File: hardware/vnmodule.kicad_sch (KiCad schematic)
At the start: 4 parts

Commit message: Fixes after review
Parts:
- R7: value 1k -> 33R
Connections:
- net GNSS_SYNC: now reaches U1.29 (GNSS_SYNC)
- net SNC_IN: no longer names the net of U1.22 (SYNC_IN)
- net SNC_OUT: no longer names the net of U1.9 (SYNC_OUT)
- no-connect marks 3 -> 4
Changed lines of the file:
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@@
+	)
+	(no_connect
+		(at 151.13 90.17)
+	)
+	(no_connect
+		(at 151.13 87.63)
 	)
 	(no_connect
@@
 		(at 151.13 78.74)
 	)
-	(no_connect
-		(at 100.33 93.98)
-	)
 	(wire
 		(pts
@@
 	(wire
 		(pts
-			(xy 157.48 90.17) (xy 151.13 90.17)
-		)
-		(stroke
-			(width 0)
-			(type default)
-		)
-	)
-	(wire
-		(pts
 			(xy 128.27 123.19) (xy 128.27 125.73)
 		)
@@
 	(wire
 		(pts
+			(xy 93.98 93.98) (xy 100.33 93.98)
+		)
+		(stroke
+			(width 0)
+			(type default)
+		)
+	)
+	(wire
+		(pts
 			(xy 64.77 91.44) (xy 64.77 95.25)
 		)
@@
 		(pts
 			(xy 125.73 123.19) (xy 125.73 125.73)
-		)
-		(stroke
-			(width 0)
-			(type default)
-		)
-	)
-	(wire
-		(pts
-			(xy 157.48 87.63) (xy 151.13 87.63)
 		)
 		(stroke
@@
 		)
 	)
-	(hierarchical_label "SNC_IN"
+	(hierarchical_label "GNSS_SYNC"
 		(shape input)
-		(at 157.48 90.17 0)
-		(effects
-			(font
-				(size 1.27 1.27)
-			)
-			(justify left)
+		(at 93.98 93.98 180)
+		(effects
+			(font
+				(size 1.27 1.27)
+			)
+			(justify right)
 		)
 	)
@@
 			)
 			(justify right)
-		)
-	)
-	(hierarchical_label "SNC_OUT"
-		(shape output)
-		(at 157.48 87.63 0)
-		(effects
-			(font
-				(size 1.27 1.27)
-			)
-			(justify left)
 		)
 	)
@@
 			)
 		)
-		(property "Value" "1k"
-			(at 162.814 101.6 90)
-			(effects
-				(font
+		(property "Value" "33R"
+			(at 163.322 101.6 90)
+			(effects
+				(font

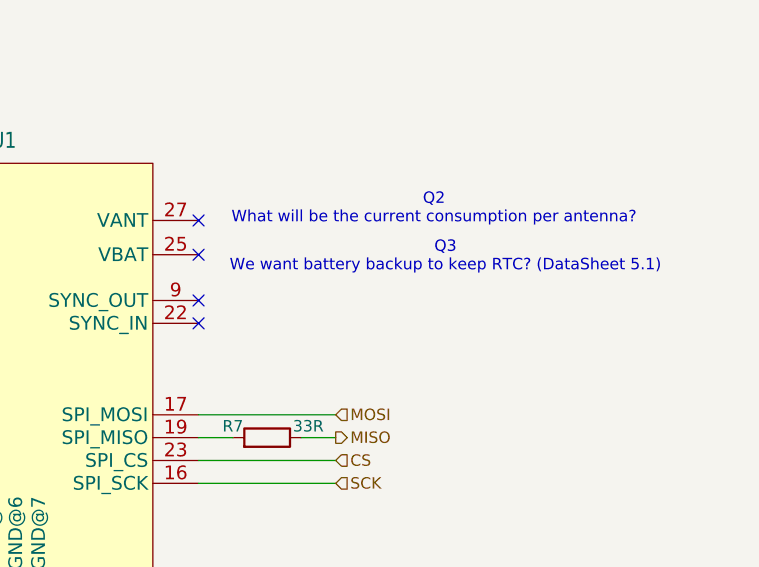
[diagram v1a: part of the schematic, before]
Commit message: Added pi-filter to VANT and added socket for battery
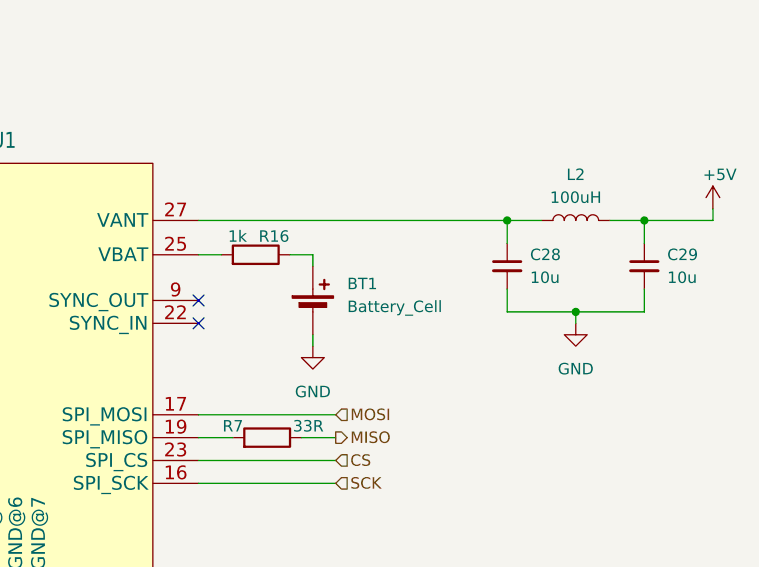
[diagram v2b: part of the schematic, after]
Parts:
- added BT1: Battery_Cell, Battery:BatteryHolder_Keystone_2998_1x6.8mm, symbol Device:Battery_Cell
- added C28, C29: 10u, 10uCap:CAPC3225X280N, symbol Device:C_Small
- added L2: 100uH, symbol Device:L
- added R16: 1k, symbol Device:R
- U1: value ~ -> (none)
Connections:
- net GND: now also BT1.2 (-), C28.2, C29.2
- net at U1.25 (VBAT): now also R16.2
- net at U1.27 (VANT): now also C28.1, L2.1
- new net: BT1.1 (+), R16.1
- new net +5V: C29.1, L2.2
- no-connect marks 4 -> 2
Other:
- note removed: "Q2 What will be the current consumption per antenna?"
- note removed: "Q3 We want battery backup to keep RTC? (DataSheet 5.1)"

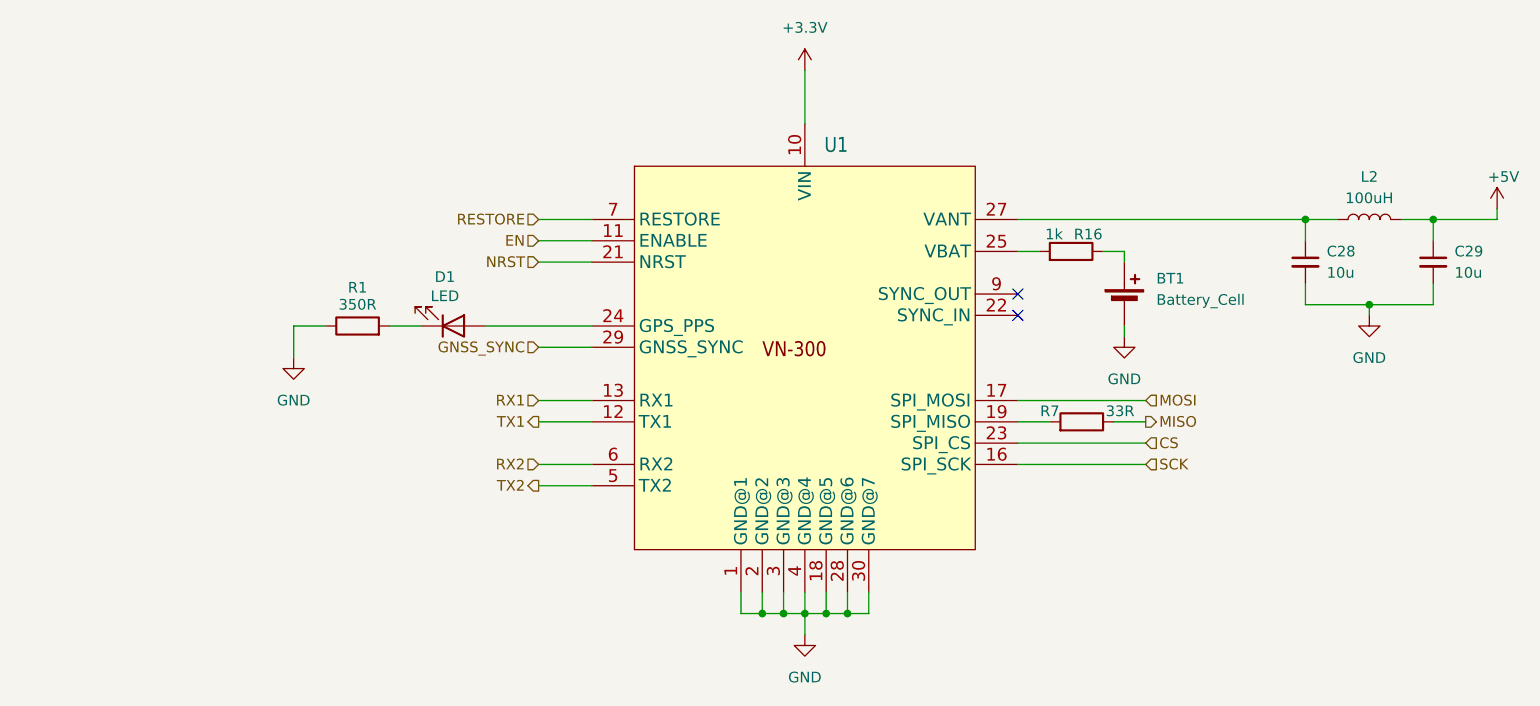
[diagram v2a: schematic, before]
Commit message: Fixes after review and mouser links for most components added
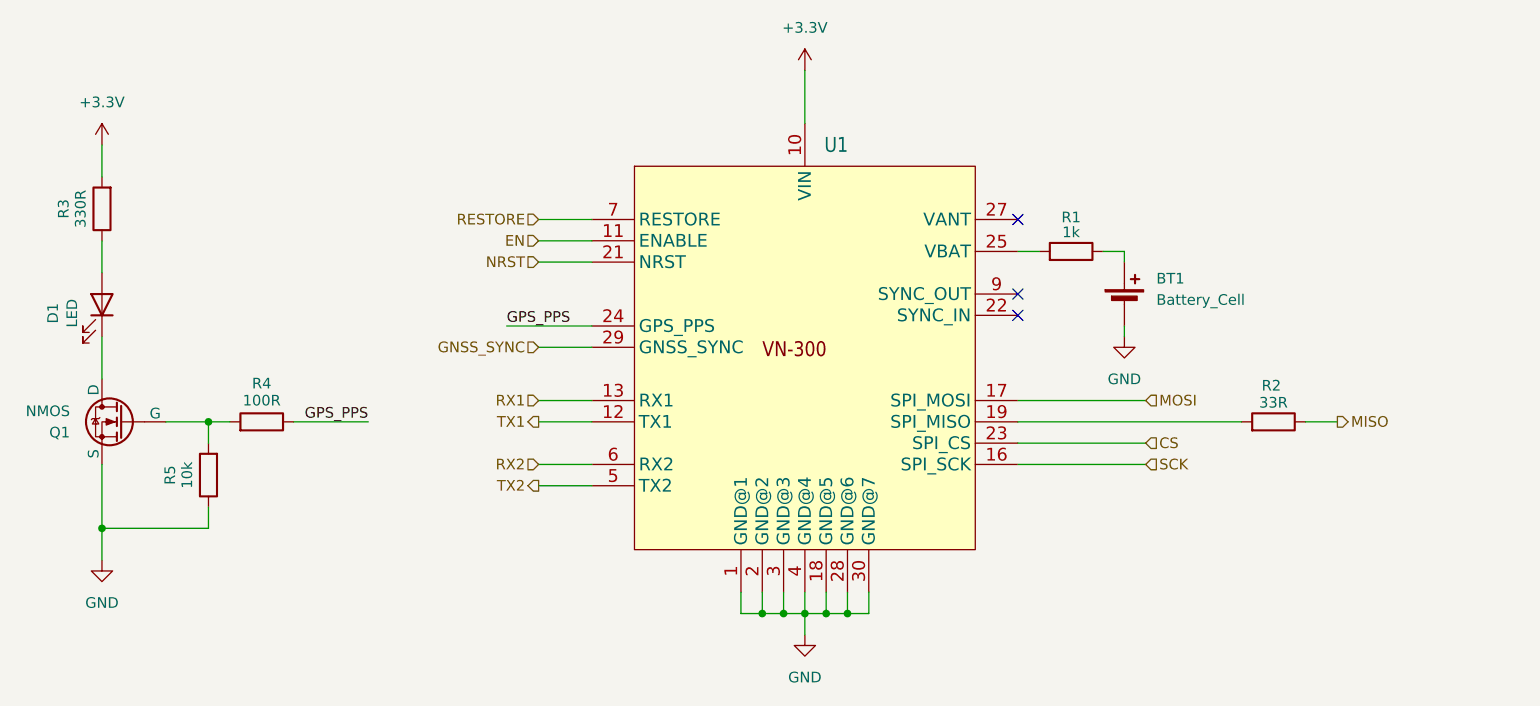
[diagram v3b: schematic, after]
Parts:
- removed C28, C29: 10u, 10uCap:CAPC3225X280N, symbol Device:C_Small
- removed L2: 100uH, symbol Device:L
- removed R1: 350R, symbol Device:R
- added Q1: NMOS, VNlednmos:DMN63D8L13, symbol Simulation_SPICE:NMOS
- added R3: 330R, Resistor_SMD:R_0603_1608Metric_Pad0.98x0.95mm_HandSolder, symbol Device:R
- added R4: 100R, Resistor_SMD:R_0603_1608Metric_Pad0.98x0.95mm_HandSolder, symbol Device:R
- added R5: 10k, Resistor_SMD:R_0603_1608Metric_Pad0.98x0.95mm_HandSolder, symbol Device:R
- R1: renamed from R16; footprint (none) -> Resistor_SMD:R_0603_1608Metric_Pad0.98x0.95mm_HandSolder; Mouser (none) -> https://www.mouser.pl/ProductDetail/Vishay/CRCW06031K00FKEE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
- R2: renamed from R7; footprint (none) -> Resistor_SMD:R_0603_1608Metric_Pad0.98x0.95mm_HandSolder; Mouser (none) -> https://www.mouser.pl/ProductDetail/YAGEO/RC0603FR-7W33RL?q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
- U1: value (none) -> VN-300; Mouser (none) -> ---
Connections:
- net +3.3V: now also R3.2
- net GND: now also Q1.3 (S), R5.1
- net at D1.1 (K): now also Q1.1 (D)
- net at D1.2 (A): now also R3.1; no longer U1.24 (GPS_PPS)
- new net: Q1.2 (G), R4.2, R5.2
- new net GPS_PPS: R4.1, U1.24 (GPS_PPS)
- no-connect marks 2 -> 3
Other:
- moved on the sheet: D1, R2

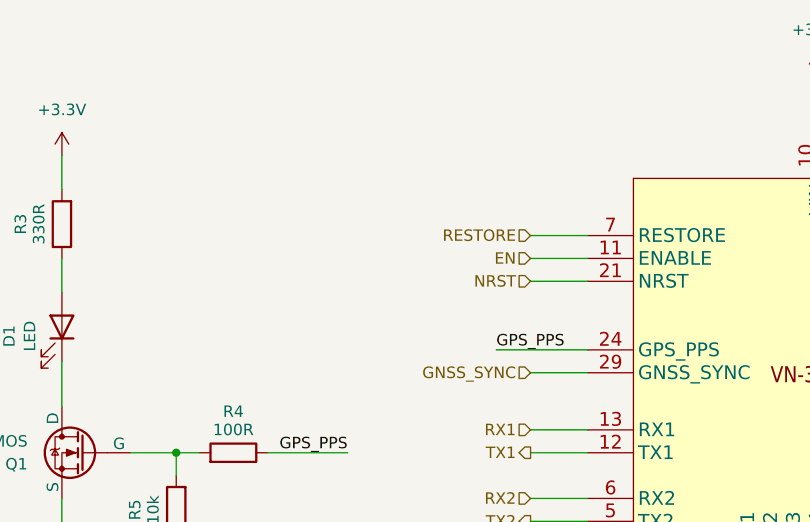
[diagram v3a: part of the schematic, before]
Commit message: changed some elements on shematic
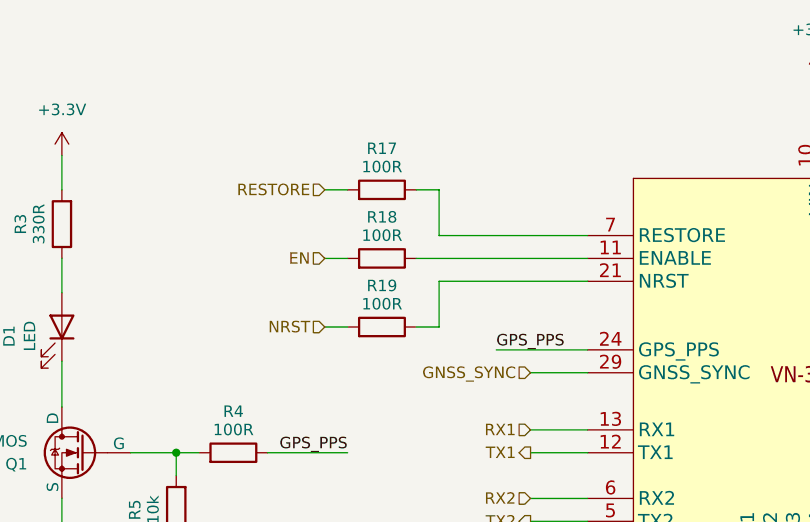
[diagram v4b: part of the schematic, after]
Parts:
- added R17, R18, R19: 100R, Resistor_SMD:R_0603_1608Metric_Pad0.98x0.95mm_HandSolder, symbol Device:R
- D1: footprint (none) -> Diode_SMD:D_0603_1608Metric_Pad1.05x0.95mm_HandSolder; Mouser (none) -> https://www.mouser.pl/ProductDetail/Wurth-Elektronik/150060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
- U1: footprint (none) -> vectornav:7X8CASTLE
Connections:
- net EN: now also R18.2; no longer U1.11 (ENABLE)
- net NRST: now also R19.2; no longer U1.21 (NRST)
- net RESTORE: now also R17.2; no longer U1.7 (RESTORE)
- new net: R18.1, U1.11 (ENABLE)
- new net: R19.1, U1.21 (NRST)
- new net: R17.1, U1.7 (RESTORE)

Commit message: 3D models, optocoupler added, pcb settings and components placing
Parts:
- BT1: footprint Battery:BatteryHolder_Keystone_2998_1x6.8mm -> BatteryHolder:2998TR; Mouser (none) -> https://www.mouser.pl/ProductDetail/Keystone-Electronics/29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
- U1: footprint vectornav:7X8CASTLE -> VN300:7X8CASTLE
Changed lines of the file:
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@@
+	)
+	(junction
+		(at 130.81 125.73)
+		(diameter 0)
+		(color 0 0 0 0)
+	)
+	(junction
+		(at 125.73 125.73)
+		(diameter 0)
+		(color 0 0 0 0)
 	)
 	(junction
@@
 	)
 	(junction
-		(at 125.73 125.73)
-		(diameter 0)
-		(color 0 0 0 0)
-	)
-	(junction
 		(at 123.19 125.73)
 		(diameter 0)
@@
 	(junction
 		(at 41.91 115.57)
-		(diameter 0)
-		(color 0 0 0 0)
-	)
-	(junction
-		(at 130.81 125.73)
 		(diameter 0)
 		(color 0 0 0 0)
@@
 			)
 		)
+		(property "Sim.Device" ""
+			(at 41.91 88.9 0)
+			(hide yes)
+			(show_name no)
+			(do_not_autoplace no)
+			(effects
+				(font
+					(size 1.27 1.27)
+				)
+			)
+		)
+		(property "Sim.Type" ""
+			(at 41.91 88.9 0)
+			(hide yes)
+			(show_name no)
+			(do_not_autoplace no)
+			(effects
+				(font
+					(size 1.27 1.27)
+				)
+			)
+		)
 		(pin "2"
 		)
@@
 			)
 		)
+		(property "Sim.Device" ""
+			(at 44.45 102.87 0)
+			(hide yes)
+			(show_name no)
+			(do_not_autoplace no)
+			(effects
+				(font
+					(size 1.27 1.27)
+				)
+			)
+		)
+		(property "Sim.Type" ""
+			(at 44.45 102.87 0)
+			(hide yes)
+			(show_name no)
+			(do_not_autoplace no)
+			(effects
+				(font
+					(size 1.27 1.27)
+				)
+			)
+		)
 		(pin "3"
 		)
@@
 		)
 		(property "Manufacturer" ""
+			(at 54.61 109.22 90)
+			(hide yes)
+			(show_name no)
+			(do_not_autoplace no)
+			(effects
+				(font
+					(size 1.27 1.27)
+				)
+			)
+		)
+		(property "Sim.Device" ""
+			(at 54.61 109.22 90)
+			(hide yes)
+			(show_name no)
+			(do_not_autoplace no)
+			(effects
+				(font
+					(size 1.27 1.27)
+				)
+			)
+		)
+		(property "Sim.Type" ""
 			(at 54.61 109.22 90)
 			(hide yes)
@@
 			)
 		)
+		(property "Sim.Device" ""
+			(at 157.48 82.55 90)
+			(hide yes)
+			(show_name no)
+			(do_not_autoplace no)
+			(effects
+				(font
+					(size 1.27 1.27)
+				)
+			)
+		)
+		(property "Sim.Type" ""
+			(at 157.48 82.55 90)
+			(hide yes)
+			(show_name no)
+			(do_not_autoplace no)
+			(effects
+				(font
+					(size 1.27 1.27)
+				)
+			)
+		)
 		(pin "2"
 		)
@@
 			)
 		)
-		(property "Footprint" "vectornav:7X8CASTLE"
+		(property "Footprint" "VN300:7X8CASTLE"
 			(at 123.952 99.314 0)
 			(hide yes)
@@
 		)
 		(property "Mouser" "---"
+			(at 125.73 95.25 0)
+			(hide yes)
+			(show_name no)
+			(do_not_autoplace no)
+			(effects
+				(font
+					(size 1.27 1.27)
+				)
+			)
+		)
+		(property "Sim.Device" ""
+			(at 125.73 95.25 0)
+			(hide yes)
+			(show_name no)
+			(do_not_autoplace no)
+			(effects
+				(font
+					(size 1.27 1.27)
+				)
+			)
+		)
+		(property "Sim.Type" ""
 			(at 125.73 95.25 0)
 			(hide yes)
@@
 			)
 		)
+		(property "Sim.Device" ""
+			(at 77.47 73.66 90)
+			(hide yes)
+			(show_name no)
+			(do_not_autoplace no)
+			(effects
+				(font
+					(size 1.27 1.27)
+				)
+			)
+		)
+		(property "Sim.Type" ""
+			(at 77.47 73.66 90)
+			(hide yes)
+			(show_name no)
+			(do_not_autoplace no)
+			(effects
+				(font
+					(size 1.27 1.27)
+				)
+			)
+		)
 		(pin "2"
 		)
@@
 			)
 		)
+		(property "Sim.Device" ""
+			(at 60.96 102.87 90)
+			(hide yes)
+			(show_name no)
+			(do_not_autoplace no)
+			(effects
+				(font
+					(size 1.27 1.27)
+				)
+			)
+		)
+		(property "Sim.Type" ""
+			(at 60.96 102.87 90)
+			(hide yes)
+			(show_name no)
+			(do_not_autoplace no)
+			(effects
+				(font
+					(size 1.27 1.27)
+				)
+			)
+		)
 		(pin "2"
 		)
@@
 			)
 		)
+		(property "Sim.Device" ""
+			(at 77.47 88.9 90)
+			(hide yes)
+			(show_name no)
+			(do_not_autoplace no)
+			(effects
+				(font
+					(size 1.27 1.27)
+				)
+			)
+		)
+		(property "Sim.Type" ""
+			(at 77.47 88.9 90)
+			(hide yes)
+			(show_name no)
+			(do_not_autoplace no)
+			(effects
+				(font
+					(size 1.27 1.27)
+				)
+			)
+		)
 		(pin "2"
 		)
@@
 		)
 		(property "Manufacturer" ""
+			(at 41.91 77.47 90)
+			(hide yes)
+			(show_name no)
+			(do_not_autoplace no)
+			(effects
+				(font
+					(size 1.27 1.27)
+				)
+			)
+		)
+		(property "Sim.Device" ""
+			(at 41.91 77.47 90)
+			(hide yes)
+			(show_name no)
+			(do_not_autoplace no)
+			(effects
+				(font
+					(size 1.27 1.27)
+				)
+			)
+		)
+		(property "Sim.Type" ""
 			(at 41.91 77.47 90)
 			(hide yes)
@@
 			)
 		)
-		(property "Footprint" "Battery:BatteryHolder_Keystone_2998_1x6.8mm"
+		(property "Footprint" "BatteryHolder:2998TR"
 			(at 163.83 87.376 90)
 			(hide yes)
@@
 			)
 		)
-		(property "Datasheet" ""
+		(property "Datasheet" "https://www.mouser.pl/datasheet/3/201/1/2998TR.pdf"
 			(at 163.83 87.376 90)
 			(hide yes)
@@
 			)
 		)
-		(property "Sim.Device" "V"
+		(property "Mouser" "https://www.mouser.pl/ProductDetail/Keystone-Electronics/2998TR?qs=xHlTOBifBJPe5POmXMwSCg%3D%3D"
 			(at 163.83 88.9 0)
 			(hide yes)
@@
 			)
 		)
-		(property "Sim.Type" "DC"
+		(property "Sim.Device" ""
 			(at 163.83 88.9 0)
 			(hide yes)
@@
 			)
 		)
-		(property "Sim.Pins" "1=+ 2=-"
-			(at 163.83 88.9 0)
-			(hide yes)
-			(show_name no)
-			(do_not_autoplace no)
-			(effects
-				(font
-					(size 1.27 1.27)
-				)
-			)
-		)
-		(property "Author" ""
-			(at 163.83 88.9 0)
-			(hide yes)
-			(show_name no)
-			(do_not_autoplace no)
-			(effects
-				(font
-					(size 1.27 1.27)
-				)
-			)
-		)
-		(property "License" ""
-			(at 163.83 88.9 0)
-			(hide yes)
-			(show_name no)
-			(do_not_autoplace no)
-			(effects
-				(font
-					(size 1.27 1.27)
-				)
-			)
-		)
-		(property "MPN" ""
-			(at 163.83 88.9 0)
-			(hide yes)
-			(show_name no)
-			(do_not_autoplace no)
-			(effects
-				(font
-					(size 1.27 1.27)
-				)
-			)
-		)
-		(property "Manufacturer" ""
+		(property "Sim.Type" ""
 			(at 163.83 88.9 0)
 			(hide yes)
@@
 			)
 		)
+		(property "Sim.Device" ""
+			(at 181.61 102.87 90)
+			(hide yes)
+			(show_name no)
+			(do_not_autoplace no)
+			(effects
+				(font
+					(size 1.27 1.27)
+				)
+			)
+		)
+		(property "Sim.Type" ""
+			(at 181.61 102.87 90)
+			(hide yes)
+			(show_name no)
+			(do_not_autoplace no)
+			(effects
+				(font
+					(size 1.27 1.27)
+				)
+			)
+		)
 		(pin "2"
 		)
@@
 			(at 77.47 81.28 90)
 			(hide yes)
+			(show_name no)
+			(do_not_autoplace no)
+			(effects
+				(font
+					(size 1.27 1.27)
+				)
+			)
+		)
+		(property "Sim.Device" ""
+			(at 77.47 81.28 90)
+			(hide yes)
+			(show_name no)
+			(do_not_autoplace no)
+			(effects
+				(font
+					(size 1.27 1.27)
+				)
+			)
+		)
+		(property "Sim.Type" ""
+			(at 77.47 81.28 90)
+			(hide yes)

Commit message: Finished routing
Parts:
- added TP8: BAT, TestPoint:TestPoint_Pad_D1.0mm, symbol Connector:TestPoint
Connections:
- net at BT1.1 (+), R1.1: now also TP8.1
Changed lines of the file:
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@@
+		(color 0 0 0 0)
+	)
+	(junction
+		(at 163.83 82.55)
+		(diameter 0)
 		(color 0 0 0 0)
 	)
@@
 					(unit 1)
 				)
+			)
+		)
+	)
+	(symbol
+		(lib_id "Connector:TestPoint")
+		(at 163.83 82.55 0)
+		(mirror y)
+		(unit 1)
+		(body_style 1)
+		(exclude_from_sim no)
+		(in_bom yes)
+		(on_board yes)
+		(in_pos_files yes)
+		(dnp no)
+		(property "Reference" "TP8"
+			(at 165.1 77.216 0)
+			(show_name no)
+			(do_not_autoplace no)
+			(effects
+				(font
+					(size 1.27 1.27)
+				)
+				(justify right)
+			)
+		)
+		(property "Value" "BAT"
+			(at 165.1 79.248 0)
+			(show_name no)
+			(do_not_autoplace no)
+			(effects
+				(font
+					(size 1.27 1.27)
+				)
+				(justify right)
+			)
+		)
+		(property "Footprint" "TestPoint:TestPoint_Pad_D1.0mm"
+			(at 158.75 82.55 0)
+			(hide yes)
+			(show_name no)
+			(do_not_autoplace no)
+			(effects
+				(font
+					(size 1.27 1.27)
+				)
+			)
+		)
+		(property "Datasheet" ""
+			(at 158.75 82.55 0)
+			(hide yes)
+			(show_name no)
+			(do_not_autoplace no)
+			(effects
+				(font
+					(size 1.27 1.27)
+				)
+			)
+		)
+		(property "Description" "test point"
+			(at 163.83 82.55 0)
+			(hide yes)
+			(show_name no)
+			(do_not_autoplace no)
+			(effects
+				(font
+					(size 1.27 1.27)
+				)
+			)
+		)
+		(pin "1"
+		)
+		(instances
+			(project "PUTM_EV_VECTORNAV"
+				(path "/b652b05a-4e3d-4ad1-b032-18886abe7d45/bf976c36-ccda-4628-98c9-d97141c7ed5e"
+					(reference "TP8")
+					(unit 1)
+				)
